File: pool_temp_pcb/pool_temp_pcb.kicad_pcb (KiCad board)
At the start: 2 copper layers, 87.6 x 57.1 mm, 9 parts, among them U1 MAX7221xNG, U2 PicoW, U3 Pool, U4 Spa

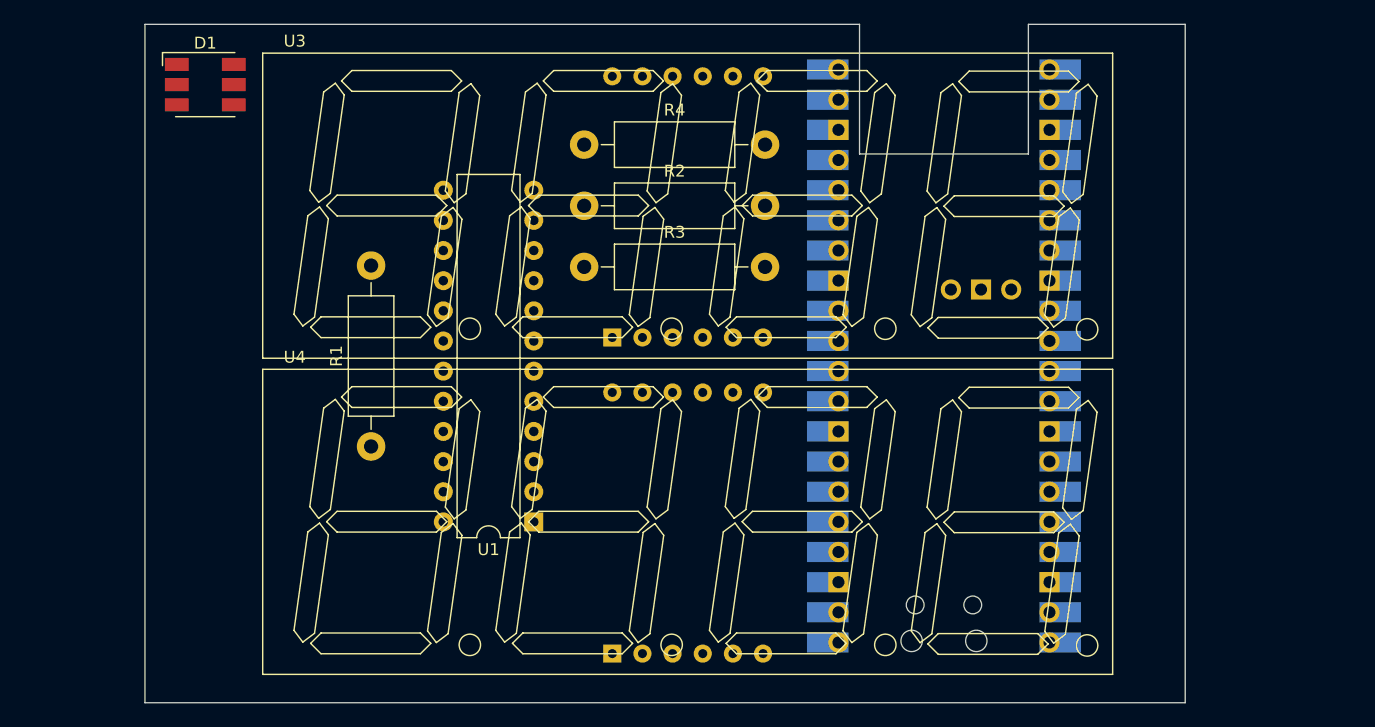
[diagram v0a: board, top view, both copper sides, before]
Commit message: Layout version 1 of temperature pcb
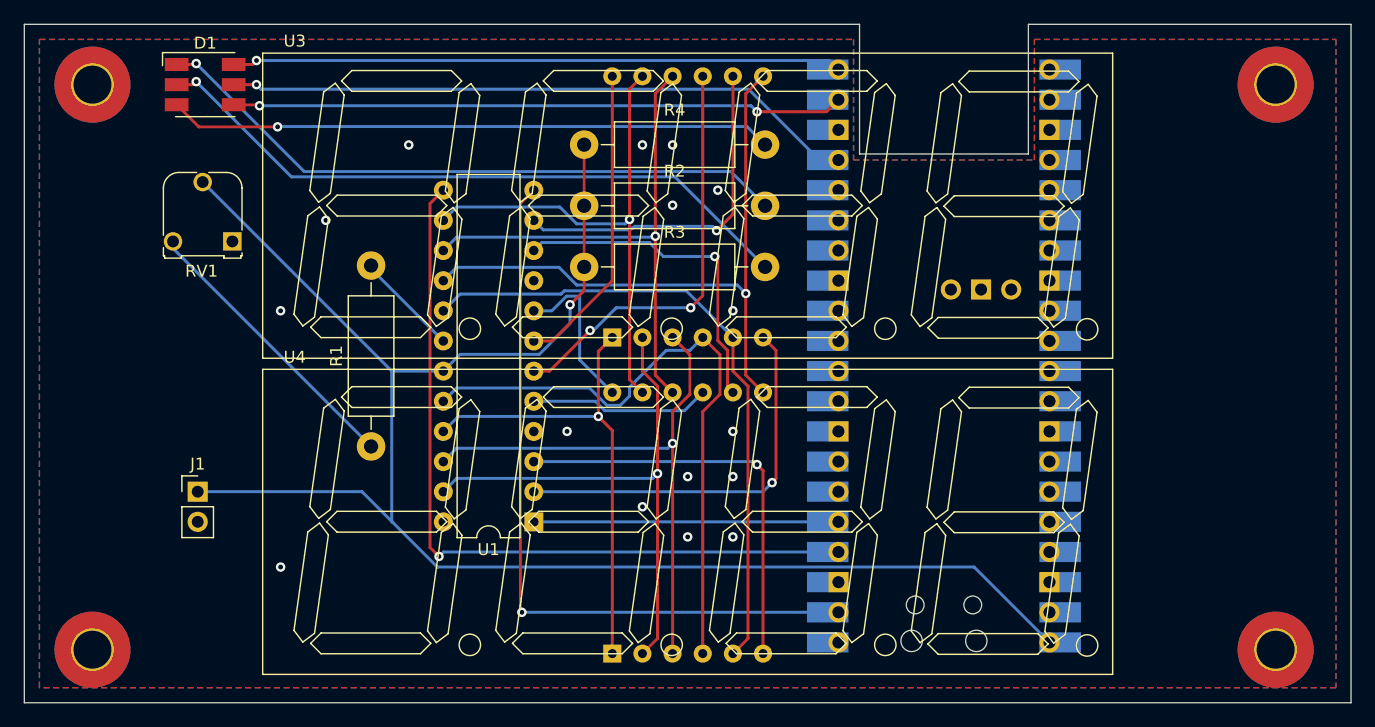
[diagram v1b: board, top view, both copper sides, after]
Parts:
- added H1: Hole, MountingHole:MountingHole_3.2mm_M3_Pad_TopBottom, F.Cu at (224.8, 111.1)
- added H2: Hole, MountingHole:MountingHole_3.2mm_M3_Pad_TopBottom, F.Cu at (125.1, 63.5)
- added H3: Hole, MountingHole:MountingHole_3.2mm_M3_Pad_TopBottom, F.Cu at (125.1, 111.1)
- added H4: Hole, MountingHole:MountingHole_3.2mm_M3_Pad_TopBottom, F.Cu at (224.8, 63.5)
- added J1: 5V, Connector_PinHeader_2.54mm:PinHeader_1x02_P2.54mm_Vertical, F.Cu at (134.0, 97.8)
- added RV1: 200k, Potentiometer_THT:Potentiometer_Runtron_RM-065_Vertical, F.Cu at (136.9, 76.7)
- D1: value Status -> AA0281
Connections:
- R1 pad 1: +5V -> Net-(R1-Pad1)
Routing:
- net +5V: track 0.00 -> 144.6 mm, vias 0 -> 1
- net SCK: track 0.00 -> 65.4 mm, vias 0 -> 1
- net CS0: track 0.00 -> 62.7 mm, vias 0 -> 1
- net Net-(D1-Pad2): track 0.00 -> 56.1 mm, vias 0 -> 1
- net SEG_{B}: track 0.00 -> 54.7 mm, vias 0 -> 1
- net Net-(D1-Pad1): track 0.00 -> 54.6 mm, vias 0 -> 1
- net SEG_{G}: track 0.00 -> 54.4 mm
- net SEG_{C}: track 0.00 -> 53.6 mm
- net RED: track 0.00 -> 53.6 mm, vias 0 -> 1
- net GREEN: track 0.00 -> 51.6 mm, vias 0 -> 2
- net BLUE: track 0.00 -> 51.4 mm, vias 0 -> 1
- net Net-(D1-Pad3): track 0.00 -> 51.0 mm, vias 0 -> 1
- net SEG_{DP}: track 0.00 -> 47.8 mm, vias 0 -> 1
- net SEG_{D}: track 0.00 -> 46.4 mm, vias 0 -> 1
- net SEG_{F}: track 0.00 -> 46.2 mm, vias 0 -> 1
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- added copper zone on B.Cu, net GND
- added copper zone on F.Cu, net GND
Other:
- board size 87.6 x 57.1 mm -> 111.8 x 57.1 mm
